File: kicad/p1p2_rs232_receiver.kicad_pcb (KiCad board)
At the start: 2 copper layers, 71.8 x 28 mm, 49 parts, among them J101 TE Connectivity 1776112-3, J102 USB_B_Mini, Q101 Q_NPN_CBE, U101 MAX22088, U102 ISO7342C, U103 CY7C65213-32LTXI

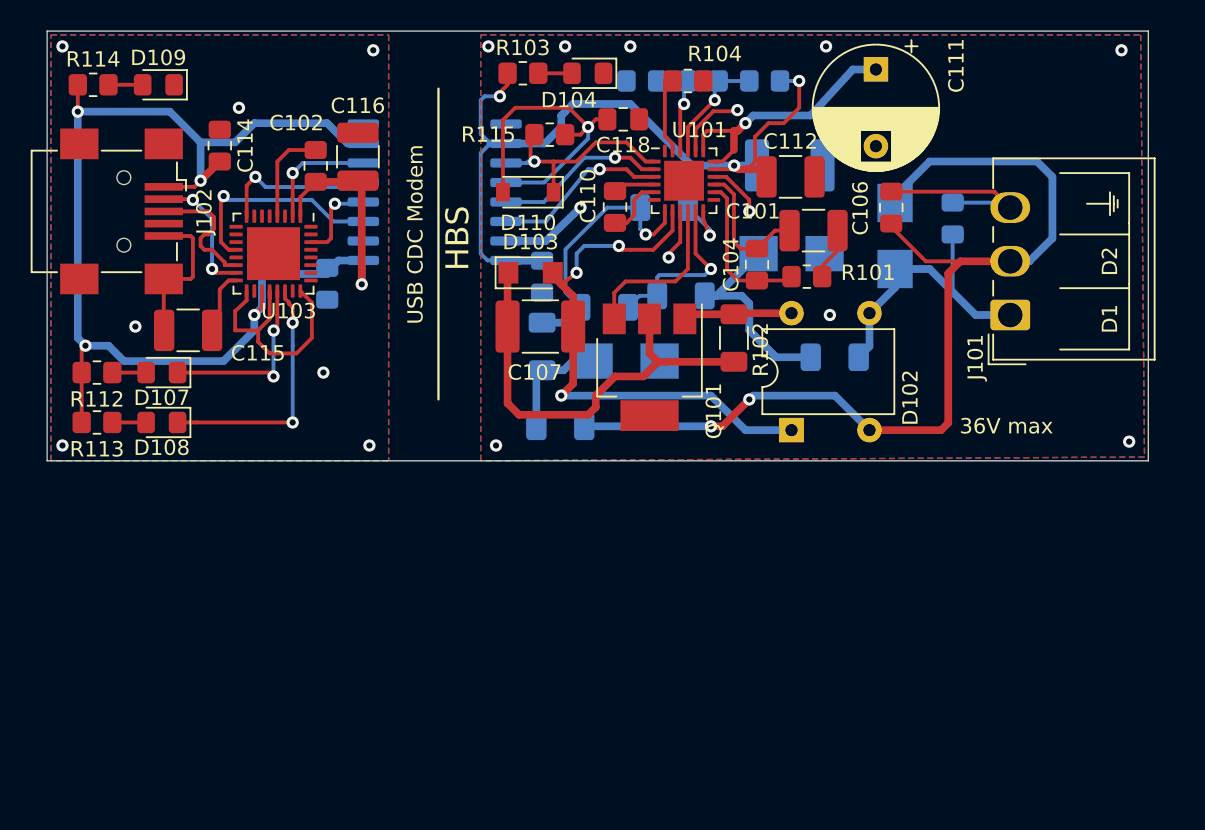
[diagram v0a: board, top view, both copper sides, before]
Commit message: pcb: Place Arduino on board
Add an Arduino to the board and a connector for external microcontrollers.
The HBS protocol requires AMI code to be transmitted, which cannot be easily
be done in hardware due to clock recovery issues.

Signed-off-by: Patrick Rudolph <siro@das-labor.org>
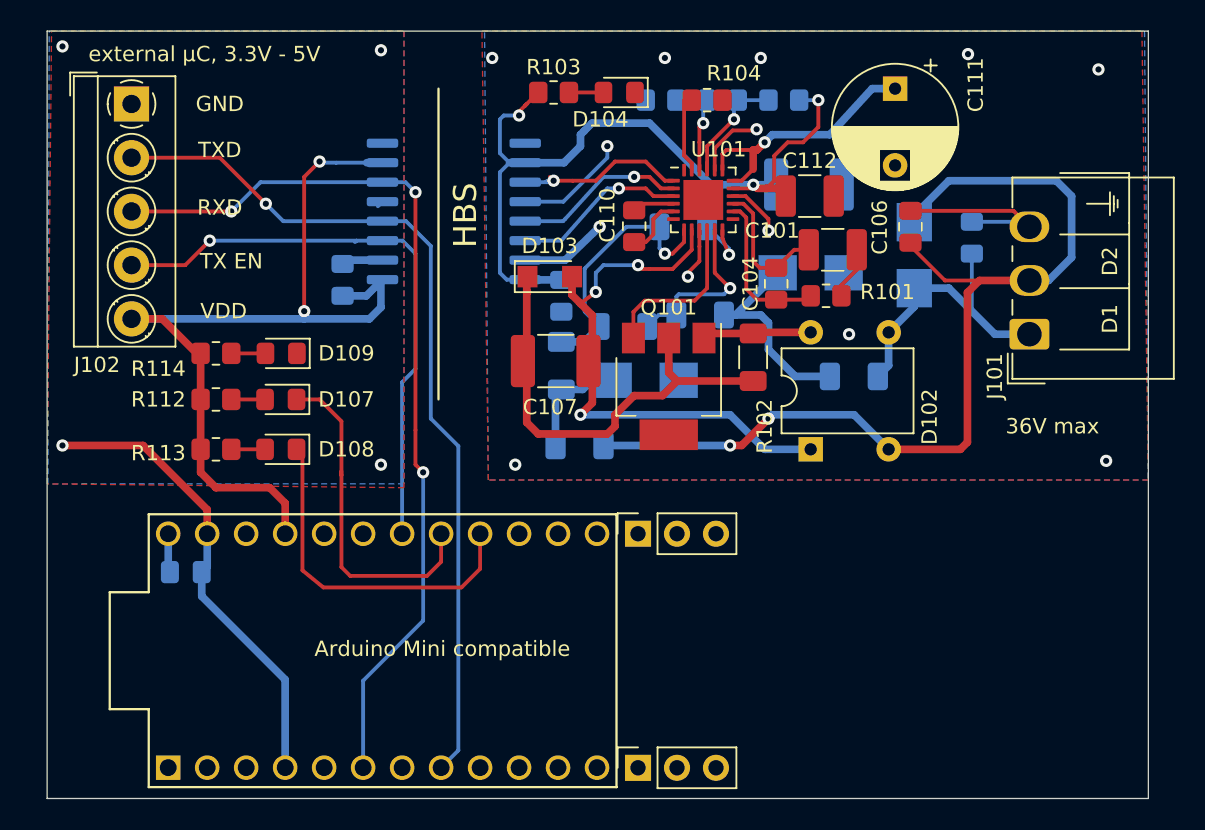
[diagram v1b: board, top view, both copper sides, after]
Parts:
- removed C115: 1u, Capacitor_SMD:C_1210_3225Metric_Pad1.33x2.70mm_HandSolder
- removed C116: 4u7, Capacitor_SMD:C_1210_3225Metric_Pad1.33x2.70mm_HandSolder
- removed C117: 100n, Capacitor_SMD:C_0805_2012Metric_Pad1.18x1.45mm_HandSolder
- removed C118: 10n, Capacitor_SMD:C_0805_2012Metric_Pad1.18x1.45mm_HandSolder
- removed D110: D_Schottky, Diode_SMD:D_SOD-123
- removed R115: 120k, Resistor_SMD:R_0805_2012Metric_Pad1.20x1.40mm_HandSolder
- added J103: Conn_01x03_Female, Connector_PinSocket_2.54mm:PinSocket_1x03_P2.54mm_Vertical, F.Cu at (140.8, 153.0)
- added J104: Conn_01x03_Female, Connector_PinSocket_2.54mm:PinSocket_1x03_P2.54mm_Vertical, F.Cu at (140.8, 137.8)
- C102, C114: moved to B.Cu
- J102: value USB_B_Mini -> Screw_Terminal_01x05; footprint Connector_USB:USB_Mini-B_Wuerth_65100516121_Horizontal -> TerminalBlock_MetzConnect:TerminalBlock_MetzConnect_Type059_RT06305HBWC_1x05_P3.50mm_Horizontal
- U103: value CY7C65213-32LTXI -> ProMicro; footprint Package_DFN_QFN:QFN-32-1EP_5x5mm_P0.5mm_EP3.45x3.45mm -> ProMicro:ProMicro
- moved C114 27.9 mm to (111.3, 140.2), turned to 180 degrees
- moved U103 26.8 mm to (124.1, 145.4), turned to 0 degrees
- moved D109 19.2 mm to (117.5, 126.0)
- moved R114 19.2 mm to (113.2, 126.0)
- moved D107 7.95 mm to (117.5, 129.0)
- moved D108 7.95 mm to (117.5, 132.2)
- moved R112 7.95 mm to (113.2, 129.0)
- moved R113 7.95 mm to (113.2, 132.2)
- moved C102 7.63 mm to (121.5, 121.2)
- moved J102 7.02 mm to (107.8, 109.8)
- moved C107 2.46 mm to (135.4, 126.5)
- moved D104 2.40 mm to (139.5, 109.0)
- moved R103 2.36 mm to (135.2, 109.0)
- moved C101 1.77 mm to (153.4, 119.2)
- moved C103 1.77 mm to (135.8, 122.2)
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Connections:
- net /~SLEEP renamed Net-(U103-Pad9)
- C102 pad 1: VBUS -> VDD
- J102 pad 1: VBUS -> GND1
- J102 pad 2: Net-(J102-Pad2) -> /TXD
- J102 pad 3: Net-(J102-Pad3) -> /RXD
- J102 pad 4: Net-(J102-Pad4) -> /TXDEN
- J102 pad 5: GND1 -> VDD
- R112 pad 1: VBUS -> VDD
- R113 pad 1: VBUS -> VDD
- R114 pad 1: VBUS -> VDD
- U102 pad 1: VBUS -> VDD
- U102 pad 12: Net-(C118-Pad2) -> GND
- U102 pad 5: /CTS -> Net-(U102-Pad5)
- U102 pad 7: VBUS -> VDD
- U103 pad 1: VBUS -> Net-(U103-Pad1)
- U103 pad 12: /TXDEN -> Net-(U103-Pad12)
- U103 pad 14: Net-(J102-Pad3) -> Net-(U103-Pad14)
- U103 pad 15: Net-(J102-Pad2) -> Net-(U103-Pad15)
- U103 pad 16: Net-(C115-Pad2) -> Net-(D108-Pad1)
- U103 pad 17: GND1 -> Net-(D107-Pad1)
- U103 pad 18: Net-(U103-Pad18) -> /TXDEN
- U103 pad 19: VBUS -> Net-(U103-Pad19)
- U103 pad 2: /RXD -> Net-(U103-Pad2)
- U103 pad 20: GND1 -> Net-(U103-Pad20)
- U103 pad 21: Net-(D107-Pad1) -> VDD
- U103 pad 22: Net-(D108-Pad1) -> Net-(U103-Pad22)
- U103 pad 23: Net-(U103-Pad23) -> GND1
- U103 pad 24: GND1 -> VBUS
- U103 pad 6: Net-(U103-Pad6) -> /RXD
- U103 pad 8: /CTS -> /TXD
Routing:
- net VBUS: track 88.4 -> 2.55 mm, vias 5 -> 0
- net VDD: track 0.00 -> 58.6 mm, vias 0 -> 2
- net /TXD: track 5.67 -> 57.2 mm
- net /RXD: track 7.68 -> 58.9 mm, vias 1 -> 3
- net /TXDEN: track 14.0 -> 38.3 mm
- net Net-(C118-Pad2): track 21.6 -> 0.00 mm, vias 1 -> 0
- net /CTS: track 10.2 -> 0.00 mm, vias 1 -> 0
- net Net-(D107-Pad1): track 12.2 -> 22.2 mm, vias 2 -> 0
- net Net-(J102-Pad3): track 8.75 -> 0.00 mm
- net Net-(J102-Pad2): track 8.60 -> 0.00 mm, vias 2 -> 0
- net GND: track 17.4 -> 24.7 mm, vias 12 -> 13
- net Net-(D108-Pad1): track 16.5 -> 22.8 mm, vias 2 -> 0
- net Net-(U101-Pad1): track 14.7 -> 11.2 mm
- net Net-(C115-Pad2): track 2.72 -> 0.00 mm
- net Net-(C107-Pad1): track 28.5 -> 29.5 mm
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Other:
- board size 71.8 x 28 mm -> 71.8 x 50 mm
- board text added: "Arduino Mini compatible"
- board text added: "GND"
- board text added: "RXD"
- board text added: "TX EN"
- board text added: "TXD"
- board text added: "VDD"
- board text added: "external µC, 3.3V - 5V"
- board text removed: "USB CDC Modem"

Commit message: Fix some issues
- Fix Q101 pinout
- Change 2k5 to 2k49 Ohm
- Change 720 to 750 Ohm

Signed-off-by: Patrick Rudolph <siro@das-labor.org>
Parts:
- Q101: value Q_NPN_CBE -> Q_NPN_BCE; footprint Package_TO_SOT_SMD:SOT-223 -> Package_TO_SOT_SMD:SOT-223-3_TabPin2
- R103, R112, R113, R114: value 720 -> 750
- R110, R111: value 2k5 -> 2k49
- moved Q101 0.30 mm to (142.4, 128.2)
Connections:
- Q101 pad 1: Net-(D102-Pad4) -> Net-(C107-Pad1)
- Q101 pad 2: Net-(C107-Pad1) -> Net-(D102-Pad4)
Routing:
- net Net-(D102-Pad4): track 7.10 -> 22.5 mm, vias 0 -> 2
- net Net-(C107-Pad1): track 29.5 -> 27.8 mm
- net GND1: vias 4 -> 10

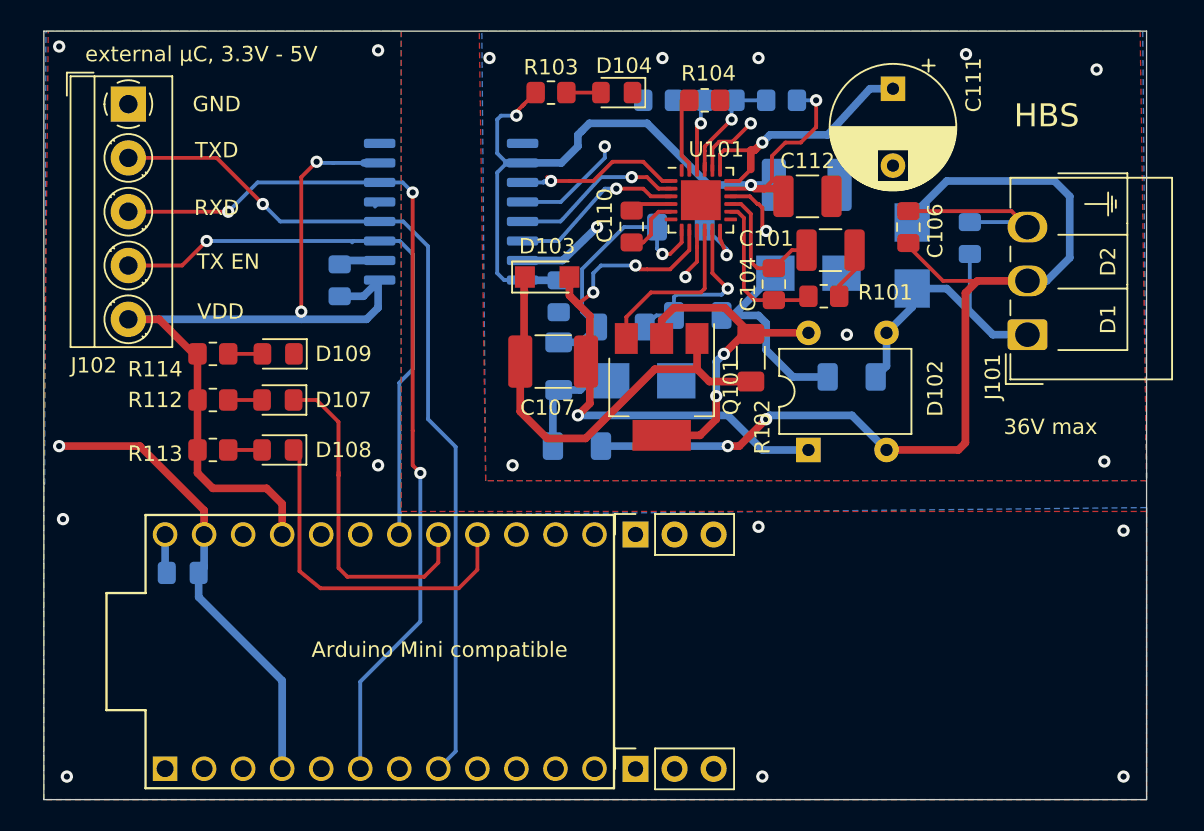
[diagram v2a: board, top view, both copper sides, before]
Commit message: pcb: Convert to standalone AMI AFE
Signed-off-by: Patrick Rudolph <patrick.rudolph@9elements.com>
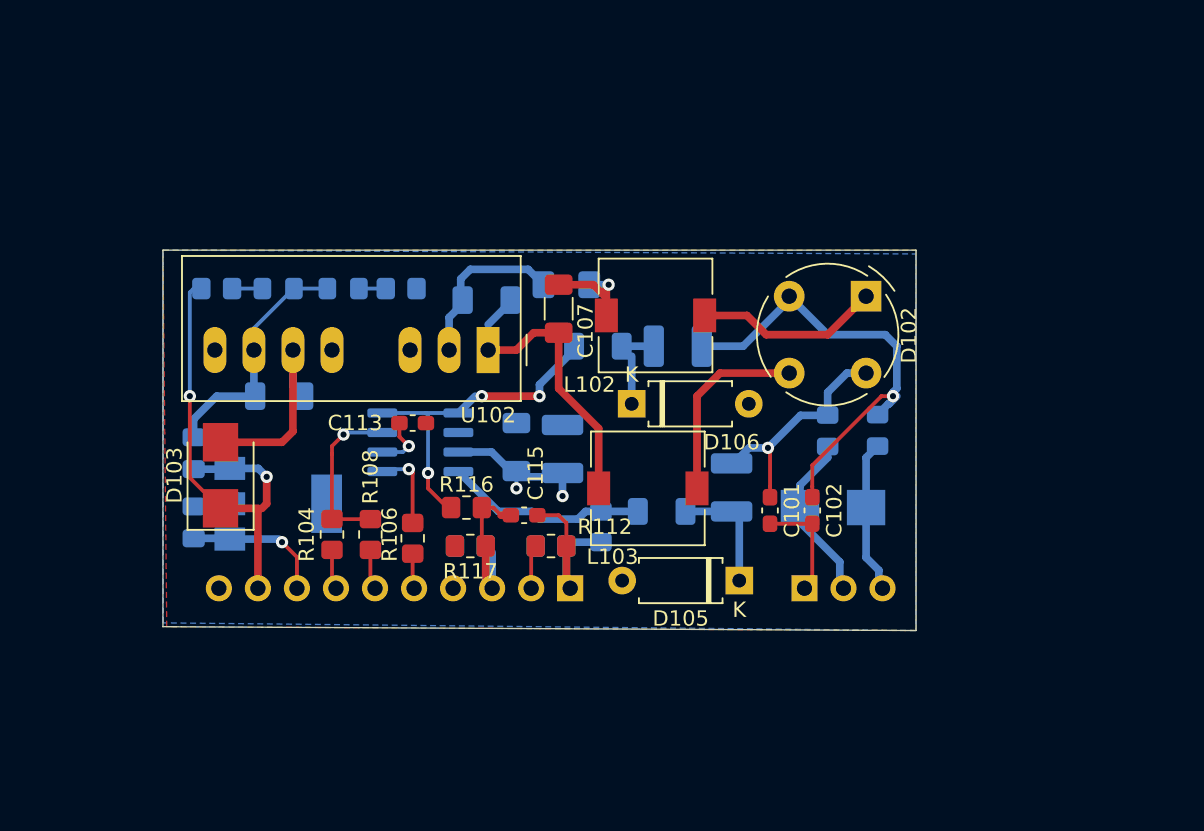
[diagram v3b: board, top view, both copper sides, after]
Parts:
- removed C108: 1u, Capacitor_SMD:C_1206_3216Metric_Pad1.33x1.80mm_HandSolder
- removed C114: 1n, Capacitor_SMD:C_0805_2012Metric_Pad1.18x1.45mm_HandSolder
- removed D108, D109: LED, LED_SMD:LED_0805_2012Metric_Pad1.15x1.40mm_HandSolder
- removed J103, J104: Conn_01x03_Female, Connector_PinSocket_2.54mm:PinSocket_1x03_P2.54mm_Vertical
- removed Q101: Q_NPN_BCE, Package_TO_SOT_SMD:SOT-223-3_TabPin2
- removed R105: 4.7, Resistor_SMD:R_1206_3216Metric_Pad1.30x1.75mm_HandSolder
- removed R111: 2k49, Resistor_SMD:R_0805_2012Metric_Pad1.20x1.40mm_HandSolder
- removed R113: 750, Resistor_SMD:R_0805_2012Metric_Pad1.20x1.40mm_HandSolder
- added C115: 6n8, Capacitor_SMD:C_0603_1608Metric_Pad1.08x0.95mm_HandSolder, F.Cu at (133.5, 136.5)
- added L101: 8u2, Inductor_SMD:L_1206_3216Metric_Pad1.42x1.75mm_HandSolder, B.Cu at (136.2, 121.5)
- added L102: PIS2812 1,0M, Inductor_SMD:L_7.3x7.3_H4.5, F.Cu at (142.1, 123.5)
- added L103: PIS2812 1,0M, Inductor_SMD:L_7.3x7.3_H4.5, F.Cu at (141.6, 134.8)
- added L104: BLM21PG 331, Inductor_SMD:L_0805_2012Metric_Pad1.15x1.40mm_HandSolder, B.Cu at (156.5, 131.0)
- added L105: BLM21PG 331, Inductor_SMD:L_0805_2012Metric_Pad1.15x1.40mm_HandSolder, B.Cu at (153.2, 131.0)
- added R116: 150, Resistor_SMD:R_0805_2012Metric_Pad1.20x1.40mm_HandSolder, F.Cu at (129.8, 136.0)
- added R117: 220, Resistor_SMD:R_0805_2012Metric_Pad1.20x1.40mm_HandSolder, F.Cu at (130.0, 138.5)
- C101: value 1u -> 1n; footprint Capacitor_SMD:C_1210_3225Metric_Pad1.33x2.70mm_HandSolder -> Capacitor_SMD:C_0603_1608Metric_Pad1.08x0.95mm_HandSolder
- C102: value 100n -> 1n; footprint Capacitor_SMD:C_0805_2012Metric_Pad1.18x1.45mm_HandSolder -> Capacitor_SMD:C_0603_1608Metric_Pad1.08x0.95mm_HandSolder; moved to F.Cu
- C103: value 100n -> 10u; footprint Capacitor_SMD:C_0805_2012Metric_Pad1.18x1.45mm_HandSolder -> Capacitor_SMD:C_1206_3216Metric_Pad1.33x1.80mm_HandSolder
- C104: value 100n -> 10u; footprint Capacitor_SMD:C_0805_2012Metric_Pad1.18x1.45mm_HandSolder -> Capacitor_SMD:C_1206_3216Metric_Pad1.33x1.80mm_HandSolder; moved to B.Cu
- C105: value 1n -> 100n
- C106: value 1n -> 2u; footprint Capacitor_SMD:C_0805_2012Metric_Pad1.18x1.45mm_HandSolder -> Capacitor_SMD:C_1206_3216Metric_Pad1.33x1.80mm_HandSolder; moved to B.Cu
- C107: value 10u -> 2u; footprint Capacitor_SMD:C_1812_4532Metric_Pad1.57x3.40mm_HandSolder -> Capacitor_SMD:C_1206_3216Metric_Pad1.33x1.80mm_HandSolder
- C109: footprint Capacitor_SMD:C_1206_3216Metric_Pad1.33x1.80mm_HandSolder -> Capacitor_SMD:C_1210_3225Metric_Pad1.33x2.70mm_HandSolder
- C110: value 100n -> 1u; footprint Capacitor_SMD:C_0805_2012Metric_Pad1.18x1.45mm_HandSolder -> Capacitor_SMD:C_1210_3225Metric_Pad1.33x2.70mm_HandSolder; moved to B.Cu
- C111: value 100u -> 10u; footprint Capacitor_THT:CP_Radial_D8.0mm_P5.00mm -> Capacitor_SMD:C_1210_3225Metric_Pad1.33x2.70mm_HandSolder; moved to B.Cu
- C112: value 1u -> 100n; footprint Capacitor_SMD:C_1210_3225Metric_Pad1.33x2.70mm_HandSolder -> Capacitor_SMD:C_0805_2012Metric_Pad1.18x1.45mm_HandSolder; moved to B.Cu
- C113: value 10u -> 100p; footprint Capacitor_SMD:C_1812_4532Metric_Pad1.57x3.40mm_HandSolder -> Capacitor_SMD:C_0603_1608Metric_Pad1.08x0.95mm_HandSolder; moved to F.Cu
- D101: value D_TVS -> SM6T 36A STM
- D102: value B80C3x00-2200A -> D_Bridge_+A-A; footprint Diode_THT:Diode_Bridge_DIP-4_W7.62mm_P5.08mm -> Diode_THT:Diode_Bridge_Round_D9.0mm
- D103: value BZD27C15P -> D_Schottky; footprint Diode_SMD:D_SMF -> Diode_SMD:D_SMB
- D104, D107, R103: moved to B.Cu
- D105, D106: value SM6T5A -> ZF 5,6; footprint Diode_SMD:D_SMB -> Diode_THT:D_A-405_P7.62mm_Horizontal; moved to F.Cu
- J101: value TE Connectivity 1776112-3 -> Conn_01x03_Female; footprint Connector_Wago:Wago_734-163_1x03_P3.50mm_Horizontal -> Connector_PinHeader_2.54mm:PinHeader_1x03_P2.54mm_Horizontal; moved to B.Cu
- J102: value Screw_Terminal_01x05 -> Conn_01x10_Female; footprint TerminalBlock_MetzConnect:TerminalBlock_MetzConnect_Type059_RT06305HBWC_1x05_P3.50mm_Horizontal -> Connector_PinSocket_2.54mm:PinSocket_1x10_P2.54mm_Horizontal; moved to B.Cu
- R101: value 180k -> 4.7; footprint Resistor_SMD:R_0805_2012Metric_Pad1.20x1.40mm_HandSolder -> Resistor_SMD:R_1206_3216Metric_Pad1.30x1.75mm_HandSolder; moved to B.Cu
- R102: value 1k -> 4.7; moved to B.Cu
- R104: value 62k -> 2k2
- R106, R108: value 200 -> 2k2; footprint Resistor_SMD:R_1206_3216Metric_Pad1.30x1.75mm_HandSolder -> Resistor_SMD:R_0805_2012Metric_Pad1.20x1.40mm_HandSolder; moved to F.Cu
- R107: value 4.7 -> 470; footprint Resistor_SMD:R_1206_3216Metric_Pad1.30x1.75mm_HandSolder -> Resistor_SMD:R_0805_2012Metric_Pad1.20x1.40mm_HandSolder
- R109: value 20k -> 220
- R110: value 2k49 -> 150
- R112: value 750 -> 220
- R114: value 750 -> 220; moved to B.Cu
- U101: value MAX22088 -> NCP1117-3.3_SOT223; footprint Package_DFN_QFN:QFN-24-1EP_4x4mm_P0.5mm_EP2.6x2.6mm -> Package_TO_SOT_SMD:SOT-223-3_TabPin2; moved to B.Cu
- U102: value ISO7342C -> TEC2-1211WI; footprint Package_SO:SOIC-16W_7.5x10.3mm_P1.27mm -> Converter_DCDC:Converter_DCDC_TRACO_TMR-xxxx_THT; moved to F.Cu
- U103: value ProMicro -> LM4861; footprint ProMicro:ProMicro -> Package_SO:SOIC-8_3.9x4.9mm_P1.27mm; moved to B.Cu
- moved C105 52.4 mm to (112.0, 132.5)
- moved C112 45.2 mm to (112.0, 137.0), turned to 90 degrees
- moved J102 42.6 mm to (136.5, 141.2), turned to 90 degrees
- moved R104 37.2 mm to (121.0, 137.8), turned to 90 degrees
- moved C102 34.2 mm to (152.2, 136.2), turned to 270 degrees
- moved U101 33.9 mm to (117.5, 135.8)
- moved C104 33.0 mm to (117.6, 128.8), turned to 180 degrees
- moved R109 32.6 mm to (135.2, 138.5), turned to 0 degrees
- moved C111 31.8 mm to (136.0, 132.2), turned to 90 degrees
- moved C113 30.0 mm to (126.2, 130.5)
- moved R110 28.8 mm to (138.5, 137.2), turned to 90 degrees
- moved R108 28.4 mm to (123.5, 137.8), turned to 270 degrees
- moved C106 27.8 mm to (131.1, 122.5), turned to 0 degrees
- moved D104 25.4 mm to (117.5, 121.8)
- moved R103 25.2 mm to (113.5, 121.8)
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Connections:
- C101 pad 2: Net-(C101-Pad2) -> Earth
- C102 pad 1: VDD -> Net-(C102-Pad1)
- C102 pad 2: GND1 -> Earth
- C103 pad 1: VCC -> +3V3
- C104 pad 2: Net-(C101-Pad2) -> GND
- C105 pad 1: Net-(C105-Pad1) -> +5V
- C105 pad 2: Net-(C105-Pad2) -> GND
- C106 pad 2: Net-(C105-Pad2) -> Net-(C106-Pad2)
- C107 pad 2: Net-(C107-Pad2) -> Net-(C106-Pad2)
- C109 pad 1: Net-(C106-Pad1) -> Net-(C102-Pad1)
- C110 pad 1: Net-(C110-Pad1) -> Net-(C101-Pad1)
- C111 pad 1: Net-(C111-Pad1) -> GND
- C111 pad 2: GND -> +3V3
- C112 pad 1: VCC -> GND
- C112 pad 2: GND -> +3V3
- C113 pad 1: VCC -> Net-(C113-Pad1)
- D101 pad 1: Net-(C105-Pad1) -> Net-(D101-Pad1)
- D101 pad 2: Net-(C106-Pad1) -> Net-(D101-Pad2)
- D102 pad 1: Net-(C107-Pad2) -> Net-(D102-Pad1)
- D102 pad 2: Net-(C106-Pad1) -> Net-(C102-Pad1)
- D102 pad 3: Net-(C105-Pad1) -> Net-(D102-Pad3)
- D102 pad 4: Net-(D102-Pad4) -> Net-(C101-Pad1)
- D103 pad 1: Net-(C107-Pad1) -> +5V
- D103 pad 2: Net-(C107-Pad2) -> Net-(C104-Pad1)
- D105 pad 1: Net-(C109-Pad2) -> Net-(C110-Pad2)
- D106 pad 1: Net-(C108-Pad2) -> Net-(C109-Pad2)
- D107 pad 1: Net-(D107-Pad1) -> GND
- J101 pad 1: Net-(C105-Pad1) -> Earth
- J101 pad 2: Net-(C106-Pad1) -> Net-(D101-Pad2)
- J101 pad 3: Net-(C105-Pad2) -> Net-(D101-Pad1)
- J102 pad 1: GND1 -> /ADC_B
- J102 pad 2: /TXD -> GND
- J102 pad 3: /RXD -> /ADC_A
- J102 pad 4: /TXDEN -> GND
- J102 pad 5: VDD -> /SHUTDOWN
- R101 pad 1: Net-(C104-Pad1) -> /A
- R101 pad 2: Net-(C101-Pad1) -> Net-(C109-Pad2)
- R102 pad 1: Net-(C107-Pad1) -> /B
- R102 pad 2: Net-(D102-Pad4) -> Net-(C110-Pad2)
- R103 pad 1: VCC -> +5V
- R104 pad 1: Net-(R104-Pad1) -> /A_H
- R104 pad 2: GND -> Net-(R104-Pad2)
- R106 pad 2: Net-(R105-Pad1) -> /SHUTDOWN
- R107 pad 1: Net-(R106-Pad1) -> +3V3
- R107 pad 2: Net-(C109-Pad2) -> Net-(D107-Pad2)
- R108 pad 1: Net-(R108-Pad1) -> Net-(R104-Pad2)
- R108 pad 2: Net-(R106-Pad1) -> /A_L
- R109 pad 1: VCC -> +3V3
- R109 pad 2: Net-(R109-Pad2) -> /ADC_B
- R110 pad 1: Net-(R109-Pad2) -> /ADC_B
- R110 pad 2: Net-(R110-Pad2) -> /B
- R112 pad 1: VDD -> /ADC_B
- R112 pad 2: Net-(D107-Pad2) -> GND
- R114 pad 1: VDD -> +3V3
- R114 pad 2: Net-(D109-Pad2) -> /ADC_A
- U101 pad 1: Net-(U101-Pad1) -> GND
- U101 pad 2: Net-(U101-Pad2) -> +3V3
- U101 pad 3: Net-(U101-Pad3) -> +5V
- U102 pad 1: VDD -> Net-(C106-Pad2)
- U102 pad 2: GND1 -> Net-(C106-Pad1)
- U102 pad 3: /TXDEN -> Net-(U102-Pad3)
- U102 pad 6: /RXD -> Net-(C104-Pad1)
- U102 pad 7: VDD -> GND
- U102 pad 8: GND1 -> Net-(U102-Pad8)
- U103 pad 1: Net-(U103-Pad1) -> Net-(R106-Pad1)
- U103 pad 2: Net-(U103-Pad2) -> Net-(C113-Pad1)
- U103 pad 3: Net-(U103-Pad3) -> Net-(R104-Pad2)
- U103 pad 4: GND1 -> /A
- U103 pad 5: Net-(U103-Pad5) -> /A
- U103 pad 6: /RXD -> +3V3
- U103 pad 7: Net-(U103-Pad7) -> GND
- U103 pad 8: /TXD -> /B
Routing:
- net /RXD: track 58.9 -> 0.00 mm, vias 3 -> 0
- net VDD: track 58.6 -> 0.00 mm, vias 2 -> 0
- net /TXD: track 57.2 -> 0.00 mm, vias 1 -> 0
- net Net-(C106-Pad1): track 65.4 -> 11.3 mm, vias 2 -> 0
- net VCC: track 51.8 -> 0.00 mm, vias 3 -> 0
- net /TXDEN: track 38.3 -> 0.00 mm, vias 1 -> 0
- net Net-(C107-Pad2): track 36.7 -> 0.00 mm, vias 3 -> 0
- net GND1: track 33.1 -> 0.00 mm, vias 10 -> 0
- net +5V: track 0.00 -> 30.8 mm, vias 0 -> 2
- net Net-(C102-Pad1): track 0.00 -> 30.4 mm, vias 0 -> 1
- net Net-(D108-Pad1): track 22.8 -> 0.00 mm
- net Net-(D102-Pad4): track 22.5 -> 0.00 mm, vias 2 -> 0
- net Net-(D107-Pad1): track 22.2 -> 0.00 mm
- net /A: track 0.00 -> 21.5 mm, vias 0 -> 3
- net Net-(C105-Pad1): track 21.3 -> 0.00 mm
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- added copper zone on B.Cu, net +3V3
- removed copper zone on B.Cu, net GND
- removed copper zone on B.Cu, net GND1
- removed copper zone on F.Cu, net GND1
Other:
- board size 71.8 x 50 mm -> 49 x 24.8 mm
- board text added: "*"
- board text removed: "36V max"
- board text removed: "Arduino Mini compatible"
- board text removed: "D1"
- board text removed: "D2"
- board text removed: "GND"
- board text removed: "HBS"
- board text removed: "RXD"
- board text removed: "TX EN"
- board text removed: "TXD"
- board text removed: "VDD"
- board text removed: "external µC, 3.3V - 5V"
